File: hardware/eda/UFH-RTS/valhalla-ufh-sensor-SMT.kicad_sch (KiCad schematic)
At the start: 53 parts, among them J1 K-TC, J2 RTD, J3 NTC, J4 1-W, J5 ModBUS, J6 ICSP, J7 MAINS, U1 ATmega328PB-A, U2 MAX31865xAP, U3 MAX31856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

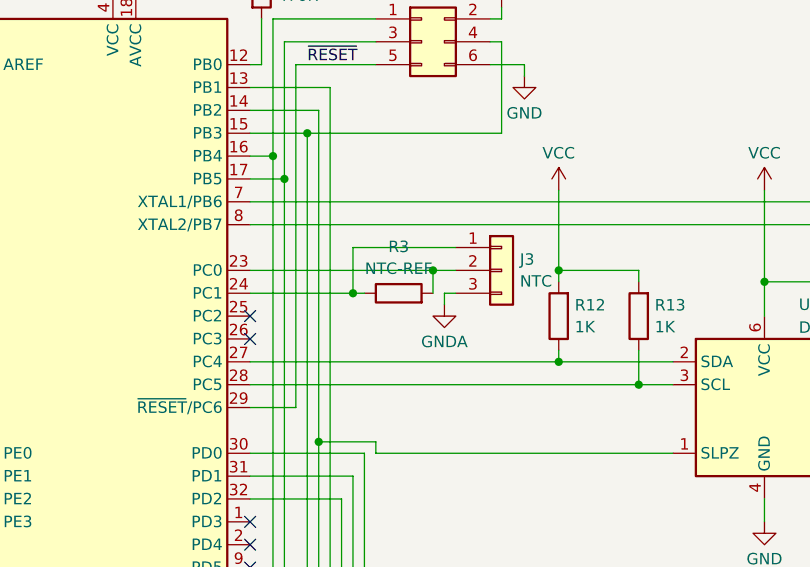
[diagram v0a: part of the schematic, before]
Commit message: BUGFIX: done cleaning-up after curved track plugin   - also switched to 2-pin terminal block for the NTC (there's no use really     in exposing the measurement power signal)
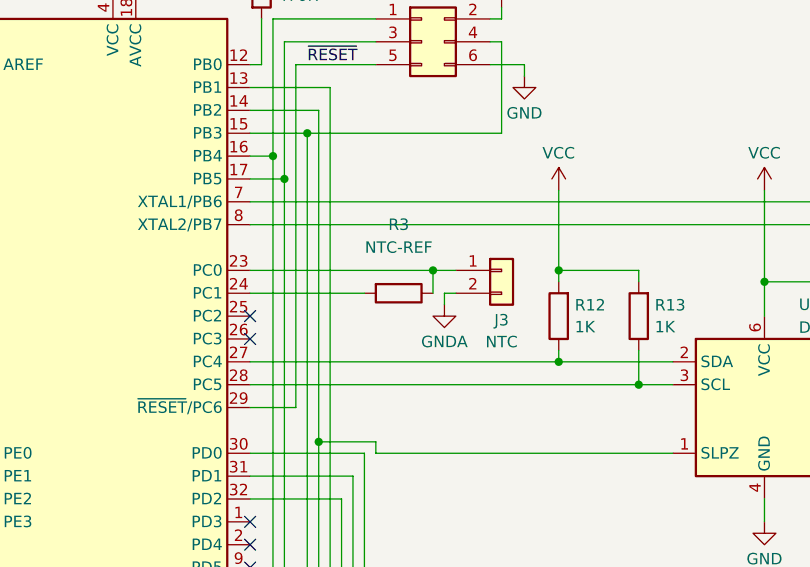
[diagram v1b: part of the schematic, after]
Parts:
- removed J3: NTC, TerminalBlock_Phoenix:TerminalBlock_Phoenix_MKDS-1,5-3-5.08_1x03_P5.08mm_Horizontal, symbol Connector_Generic:Conn_01x03
- added J3: NTC, TerminalBlock_Phoenix:TerminalBlock_Phoenix_MKDS-1,5-2-5.08_1x02_P5.08mm_Horizontal, symbol Connector_Generic:Conn_01x02
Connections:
- net GNDA: now also J3.2 (Pin_2)
- net at U1.23 (PC0): now also R3.1, J3.1 (Pin_1); no longer R3.2
- net at U1.24 (PC1): now also R3.2; no longer R3.1
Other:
- moved on the sheet: R3
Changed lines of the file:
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@@
   (junction (at 151.13 153.67) (diameter 0) (color 0 0 0 0)
   )
-  (junction (at 177.8 109.22) (diameter 0) (color 0 0 0 0)
-  )
   (junction (at 196.85 229.87) (diameter 0) (color 0 0 0 0)
   )
@@
     (stroke (width 0) (type default))
   )
-  (wire (pts (xy 177.8 104.14) (xy 177.8 109.22))
-    (stroke (width 0) (type default))
-  )
   (wire (pts (xy 166.37 127) (xy 179.07 127))
     (stroke (width 0) (type default))
@@
     (stroke (width 0) (type default))
   )
-  (wire (pts (xy 189.23 104.14) (xy 177.8 104.14))
-    (stroke (width 0) (type default))
-  )
   (wire (pts (xy 232.41 229.87) (xy 201.93 229.87))
     (stroke (width 0) (type default))
@@
     (stroke (width 0) (type default))
   )
-  (wire (pts (xy 166.37 109.22) (xy 177.8 109.22))
-    (stroke (width 0) (type default))
-  )
   (wire (pts (xy 180.34 127) (xy 180.34 125.73))
     (stroke (width 0) (type default))
@@
     (stroke (width 0) (type default))
   )
-  (wire (pts (xy 177.8 109.22) (xy 179.07 109.22))
+  (wire (pts (xy 166.37 109.22) (xy 179.07 109.22))
     (stroke (width 0) (type default))
   )
@@
     )
   )
-  (symbol (lib_id "Device:R") (at 182.88 109.22 90) (unit 1)
+  (symbol (lib_id "Device:R") (at 182.88 109.22 270) (unit 1)
     (in_bom yes) (on_board yes) (dnp no) (fields_autoplaced)
-    (property "Reference" "R3" (at 182.88 104.0597 90)
+    (property "Reference" "R3" (at 182.88 101.6 90)
       (effects (font (size 1.27 1.27)))
     )
-    (property "Value" "NTC-REF" (at 182.88 106.4839 90)
+    (property "Value" "NTC-REF" (at 182.88 104.14 90)
       (effects (font (size 1.27 1.27)))
     )
-    (property "Footprint" "Resistor_SMD:R_1206_3216Metric" (at 182.88 110.998 90)
+    (property "Footprint" "Resistor_SMD:R_1206_3216Metric" (at 182.88 107.442 90)
       (effects (font (size 1.27 1.27)) hide)
     )
@@
     )
   )
-  (symbol (lib_id "Connector_Generic:Conn_01x03") (at 194.31 106.68 0) (unit 1)
-    (in_bom yes) (on_board yes) (dnp no) (fields_autoplaced)
-    (property "Reference" "J3" (at 196.342 105.4679 0)
-      (effects (font (size 1.27 1.27)) (justify left))
-    )
-    (property "Value" "NTC" (at 196.342 107.8921 0)
-      (effects (font (size 1.27 1.27)) (justify left))
-    )
-    (property "Footprint" "TerminalBlock_Phoenix:TerminalBlock_Phoenix_MKDS-1,5-3-5.08_1x03_P5.08mm_Horizontal" (at 194.31 106.68 0)
-      (effects (font (size 1.27 1.27)) hide)
-    )
-    (property "Datasheet" "~" (at 194.31 106.68 0)
-      (effects (font (size 1.27 1.27)) hide)
-    )
-    (pin "1")
-    (pin "2")
-    (pin "3")
-    (instances
-      (project "valhalla-ufh-sensor-SMT"
-        (path "/e7b68850-8d2b-4865-b2bd-a32c4325e4e6"
-          (reference "J3") (unit 1)
-        )
-      )
-    )
-  )
   (symbol (lib_id "power:GNDA") (at 187.96 110.49 0) (unit 1)
     (in_bom yes) (on_board yes) (dnp no) (fields_autoplaced)
@@
         )
       )
+    )
+  )
+  (symbol (lib_id "Connector_Generic:Conn_01x02") (at 194.31 106.68 0) (unit 1)
+    (in_bom yes) (on_board yes) (dnp no) (fields_autoplaced)
+    (property "Reference" "J3" (at 194.31 112.2101 0)
+      (effects (font (size 1.27 1.27)))
+    )
+    (property "Value" "NTC" (at 194.31 114.6343 0)
+      (effects (font (size 1.27 1.27)))
+    )
+    (property "Footprint" "TerminalBlock_Phoenix:TerminalBlock_Phoenix_MKDS-1,5-2-5.08_1x02_P5.08mm_Horizontal" (at 194.31 106.68 0)
+      (effects (font (size 1.27 1.27)) hide)
+    )
+    (property "Datasheet" "~" (at 194.31 106.68 0)
+      (effects (font (size 1.27 1.27)) hide)
+    )
+    (pin "2")
+    (pin "1")
+    (instances
+      (project "valhalla-ufh-sensor-SMT"
+        (path "/e7b68850-8d2b-4865-b2bd-a32c4325e4e6"
+          (reference "J3") (unit 1)
+        )
+      )

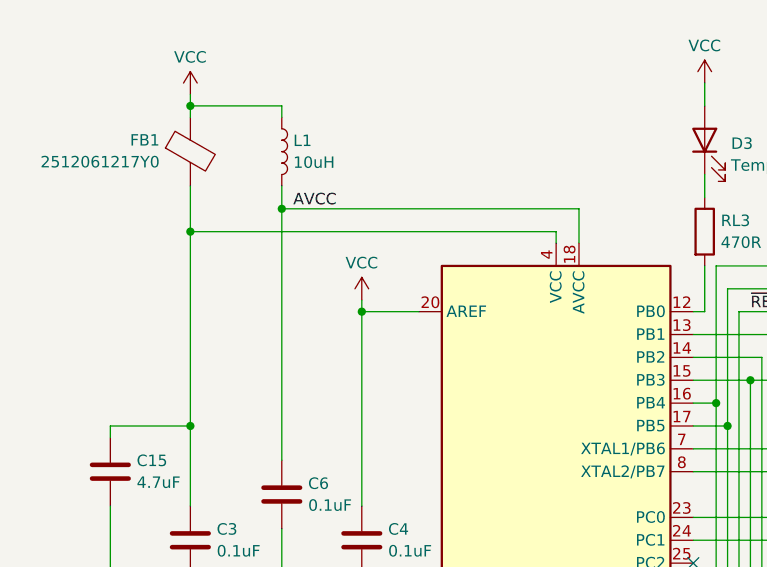
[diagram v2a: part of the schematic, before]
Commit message: UPDATE: fixed connection of AREF on UFH CPU
 - according to official documentation, ATMega's AREF pin should be
   connected only to a decoupling capacitor. If/when AREF=AVCC is
   desired for an ADC measurement, they can be connected together
   internally via register settings.
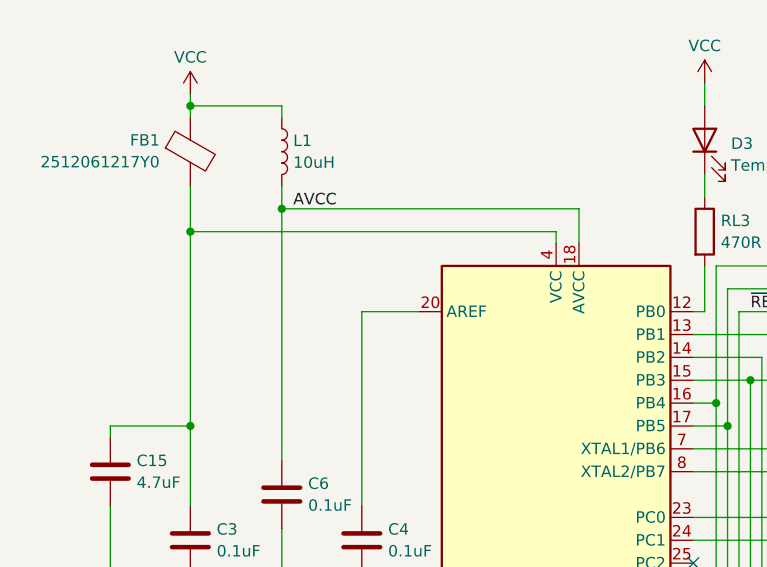
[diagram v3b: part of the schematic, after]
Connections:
- net VCC: no longer C4.1, U1.20 (AREF)
- new net: C4.1, U1.20 (AREF)
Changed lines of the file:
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@@
 	)
 	(junction
-		(at 129.54 83.82)
-		(diameter 0)
-		(color 0 0 0 0)
-	)
-	(junction
 		(at 170.18 200.66)
 		(diameter 0)
@@
 	(wire
 		(pts
-			(xy 129.54 82.55) (xy 129.54 83.82)
-		)
-		(stroke
-			(width 0)
-			(type default)
-		)
-	)
-	(wire
-		(pts
 			(xy 300.99 134.62) (xy 278.13 134.62)
 		)
@@
 	(wire
 		(pts
+			(xy 129.54 83.82) (xy 135.89 83.82)
+		)
+		(stroke
+			(width 0)
+			(type default)
+		)
+	)
+	(wire
+		(pts
 			(xy 234.95 124.46) (xy 234.95 125.73)
 		)
@@
 	(wire
 		(pts
-			(xy 129.54 83.82) (xy 135.89 83.82)
-		)
-		(stroke
-			(width 0)
-			(type default)
-		)
-	)
-	(wire
-		(pts
 			(xy 289.56 114.3) (xy 289.56 139.7)
 		)
@@
 					(unit 1)
 				)
-			)
-		)
-	)
-	(symbol
-		(lib_id "power:VCC")
-		(at 129.54 82.55 0)
-		(unit 1)
-		(exclude_from_sim no)
-		(in_bom yes)
-		(on_board yes)
-		(dnp no)
-		(fields_autoplaced yes)
-		(property "Reference" "#PWR025"
-			(at 129.54 86.36 0)
-			(effects
-				(font
-					(size 1.27 1.27)
-				)
-				(hide yes)
-			)
-		)
-		(property "Value" "VCC"
-			(at 129.54 78.4169 0)
-			(effects
-				(font
-					(size 1.27 1.27)
-				)
-			)
-		)
-		(property "Footprint" ""
-			(at 129.54 82.55 0)
-			(effects
-				(font
-					(size 1.27 1.27)
-				)
-				(hide yes)
-			)
-		)
-		(property "Datasheet" ""
-			(at 129.54 82.55 0)
-			(effects
-				(font
-					(size 1.27 1.27)
-				)
-				(hide yes)
-			)
-		)
-		(property "Description" ""
-			(at 129.54 82.55 0)
-			(effects
-				(font
-					(size 1.27 1.27)
-				)
-				(hide yes)
-			)
-		)
-		(pin "1"
-		)
-		(instances
-			(project "valhalla-ufh-sensor-SMT"
-				(path "/e7b68850-8d2b-4865-b2bd-a32c4325e4e6"
-					(reference "#PWR025")
-					(unit 1)
-				)
